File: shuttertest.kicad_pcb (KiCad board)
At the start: 2 copper layers, 52 x 101.3 mm, 74 parts, among them J1 Conn_01x20_Female, J2 Conn_01x06_Male, J3 Conn_01x06_Female, J4 Conn_01x06_Female, J5 Conn_01x06_Male, J6 Conn_01x06_Female, J7 Conn_01x06_Female, J8 AVR-ISP-6, SW1 SW_Push, U1 ATmega328PB-A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

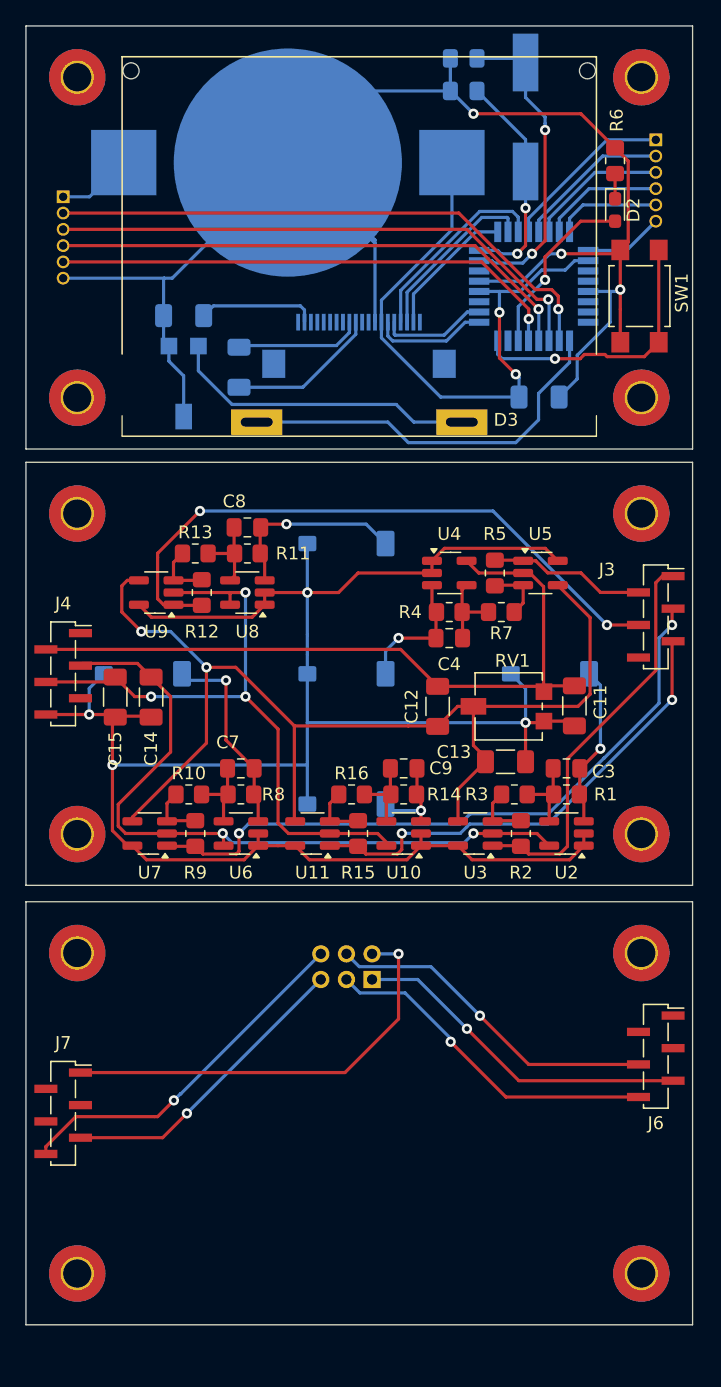
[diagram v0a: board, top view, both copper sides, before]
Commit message: Use through-hole connectors on bottom board
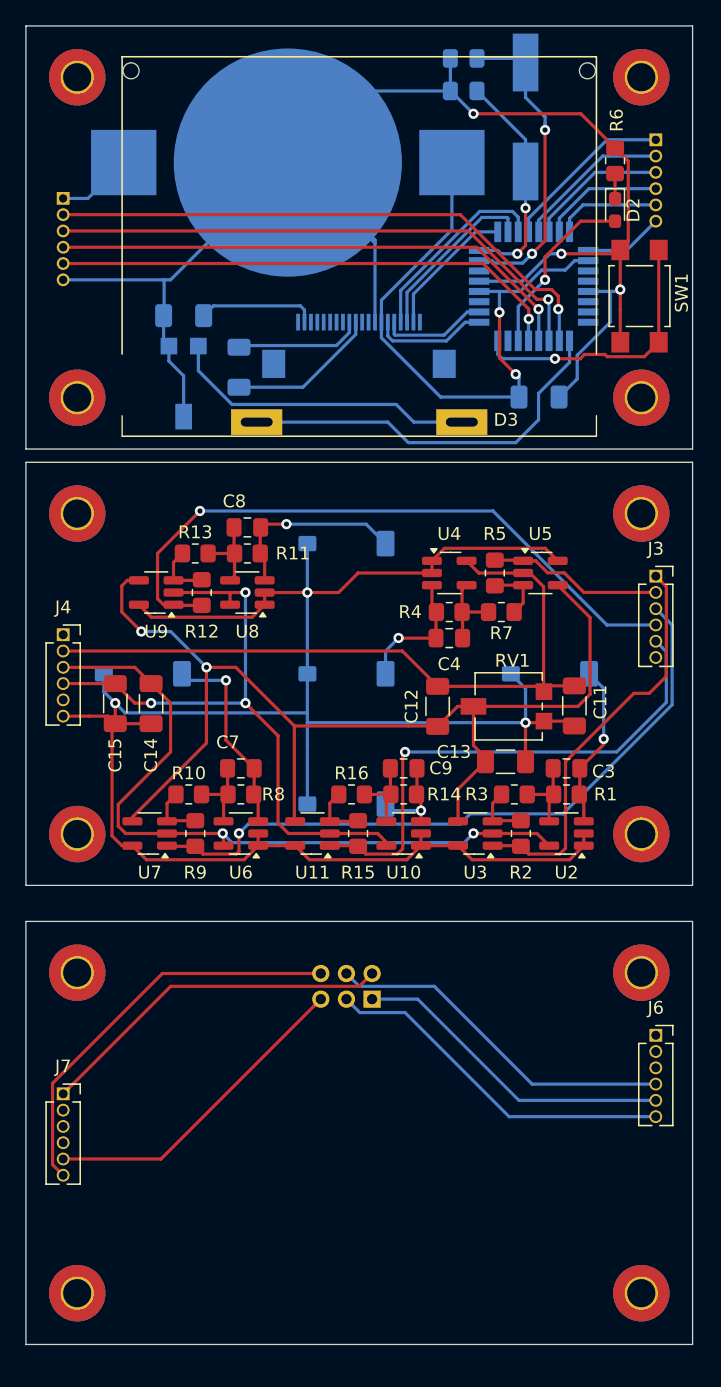
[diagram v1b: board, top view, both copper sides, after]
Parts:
- J3, J4, J6, J7: footprint Connector_PinSocket_1.27mm:PinSocket_1x06_P1.27mm_Vertical_SMD_Pin1Right -> Connector_PinSocket_1.27mm:PinSocket_1x06_P1.27mm_Vertical
- moved J3 3.18 mm to (124.0, 78.7)
- moved J4 3.05 mm to (77.7, 83.3)
- moved J6 1.64 mm to (124.0, 114.6)
- moved REF** 1.53 mm to (78.8, 134.7)
- moved REF** 1.53 mm to (122.8, 134.7)
- moved J8 1.53 mm to (101.8, 111.7)
- moved REF** 1.53 mm to (78.8, 109.7)
- moved REF** 1.53 mm to (122.8, 109.7)
- moved J7 1.51 mm to (77.7, 119.1)
- moved C14 0.51 mm to (84.6, 88.7)
- moved C15 0.51 mm to (81.8, 88.7)
- moved J5 0.13 mm to (77.7, 49.3)
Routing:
- net VDD: track 33.7 -> 28.0 mm, vias 1 -> 0
- net GND2: track 28.3 -> 32.0 mm, vias 1 -> 0
- net Net-(J3-Pin_5): track 37.2 -> 40.8 mm, vias 2 -> 1
- net unconnected-(C15-Pad1): track 51.4 -> 49.9 mm
- net VCC: track 57.9 -> 56.5 mm
- net unconnected-(J7-Pin_5-Pad5): track 23.9 -> 25.3 mm, vias 1 -> 0
- net Net-(J6-Pin_5): track 26.8 -> 25.4 mm, vias 1 -> 0
- net Net-(J6-Pin_4): track 26.4 -> 27.7 mm, vias 1 -> 0
- net Net-(J3-Pin_2): track 12.2 -> 13.6 mm
- net GND1: track 166.0 -> 164.8 mm, vias 4 -> 3
- net unconnected-(J6-Pin_6-Pad6): track 26.7 -> 27.9 mm, vias 1 -> 0
- net Net-(J3-Pin_3): track 52.2 -> 53.3 mm, vias 2 -> 1
- net unconnected-(C14-Pad1): track 56.4 -> 57.3 mm
- net Net-(J3-Pin_4): track 50.5 -> 51.1 mm, vias 2 -> 1
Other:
- board size 52 x 101.3 mm -> 52 x 102.9 mm

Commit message: Unify panel gap
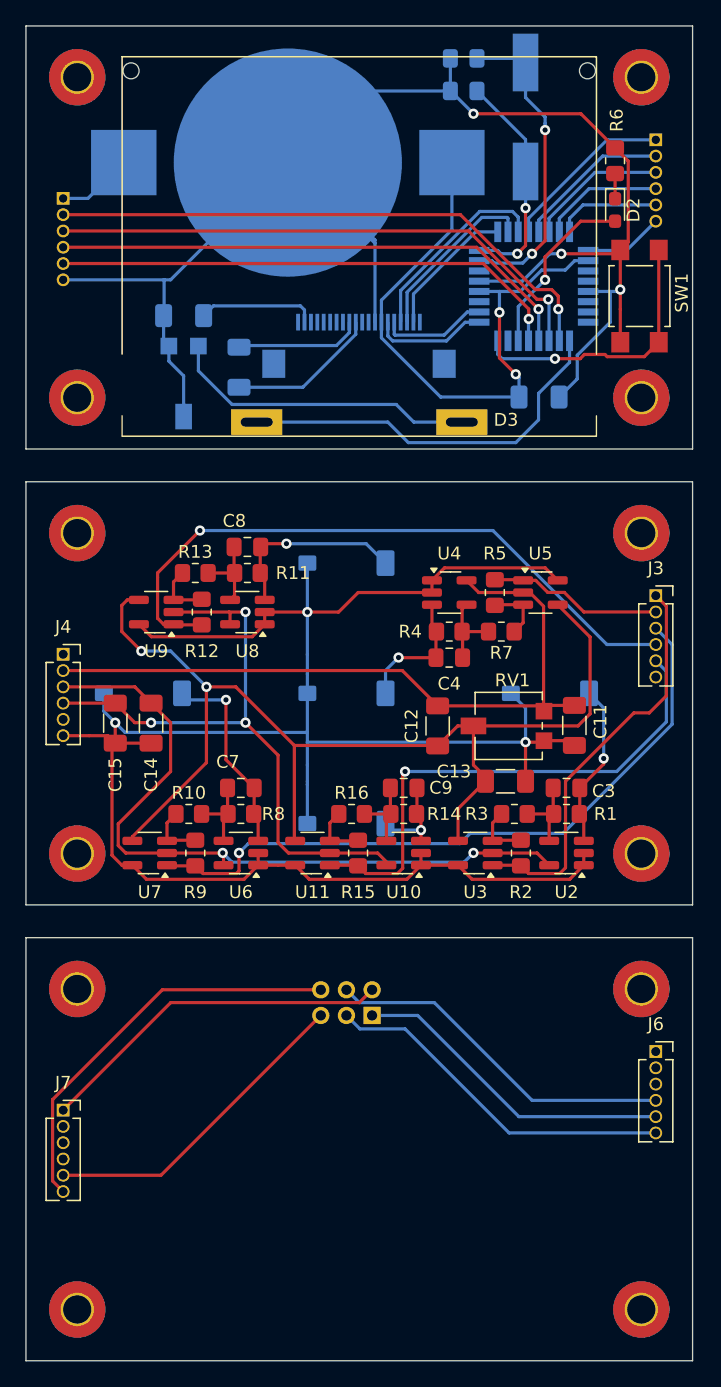
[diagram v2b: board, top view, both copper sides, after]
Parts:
- moved C12 1.52 mm to (106.9, 90.4)
- moved C13 1.52 mm to (112.2, 94.7)
- moved C14 1.52 mm to (84.6, 90.2)
- moved C15 1.52 mm to (81.8, 90.2)
- moved C3 1.52 mm to (117.0, 95.3)
- moved C4 1.52 mm to (107.8, 85.1)
- moved C7 1.52 mm to (91.6, 95.3)
- moved C8 1.52 mm to (92.1, 76.5)
- moved C9 1.52 mm to (104.3, 95.3)
- moved D1 1.52 mm to (115.7, 87.9)
- moved D4 1.52 mm to (99.8, 87.9)
- moved D5 1.52 mm to (83.9, 87.9)
- moved D6 1.52 mm to (99.8, 77.7)
- moved D7 1.52 mm to (99.8, 98.0)
- moved J3 1.52 mm to (124.0, 80.3)
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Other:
- board size 52 x 102.9 mm -> 52 x 104.1 mm

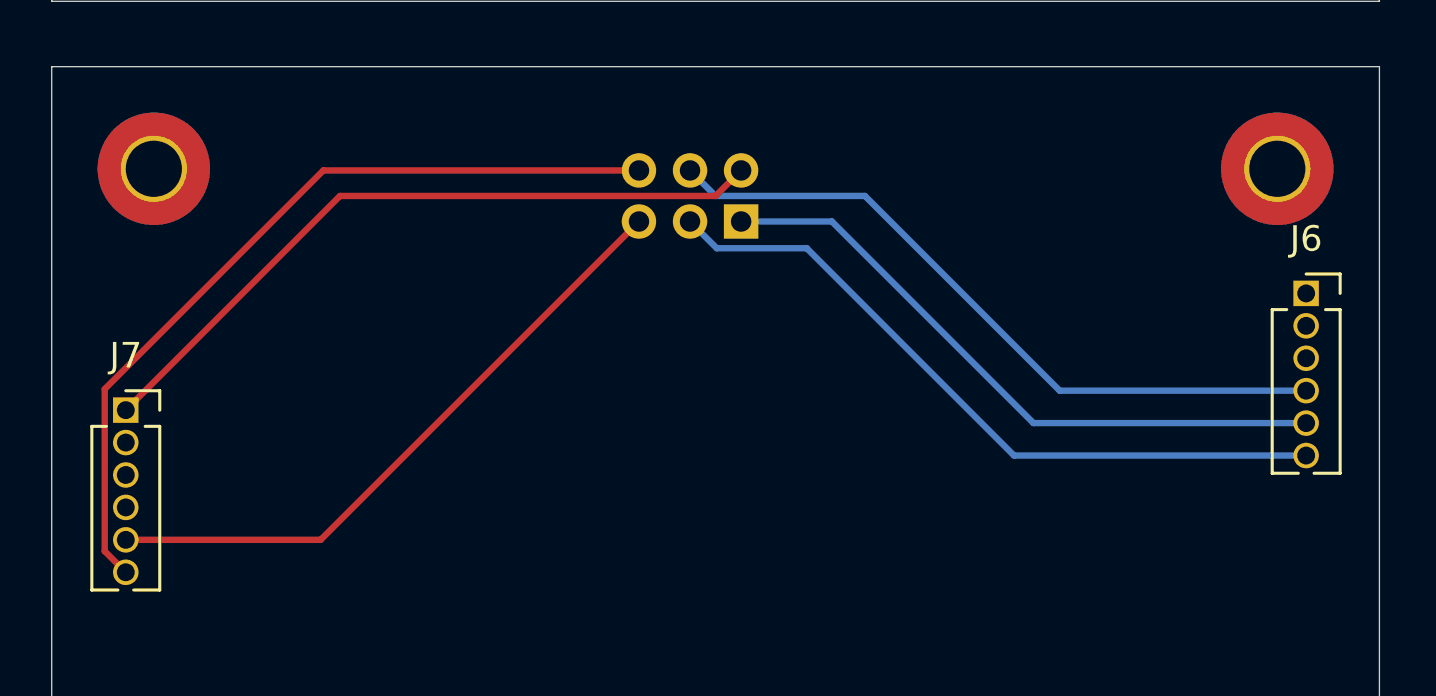
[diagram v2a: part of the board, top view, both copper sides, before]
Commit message: 2.54mm pitch AVR ISP header
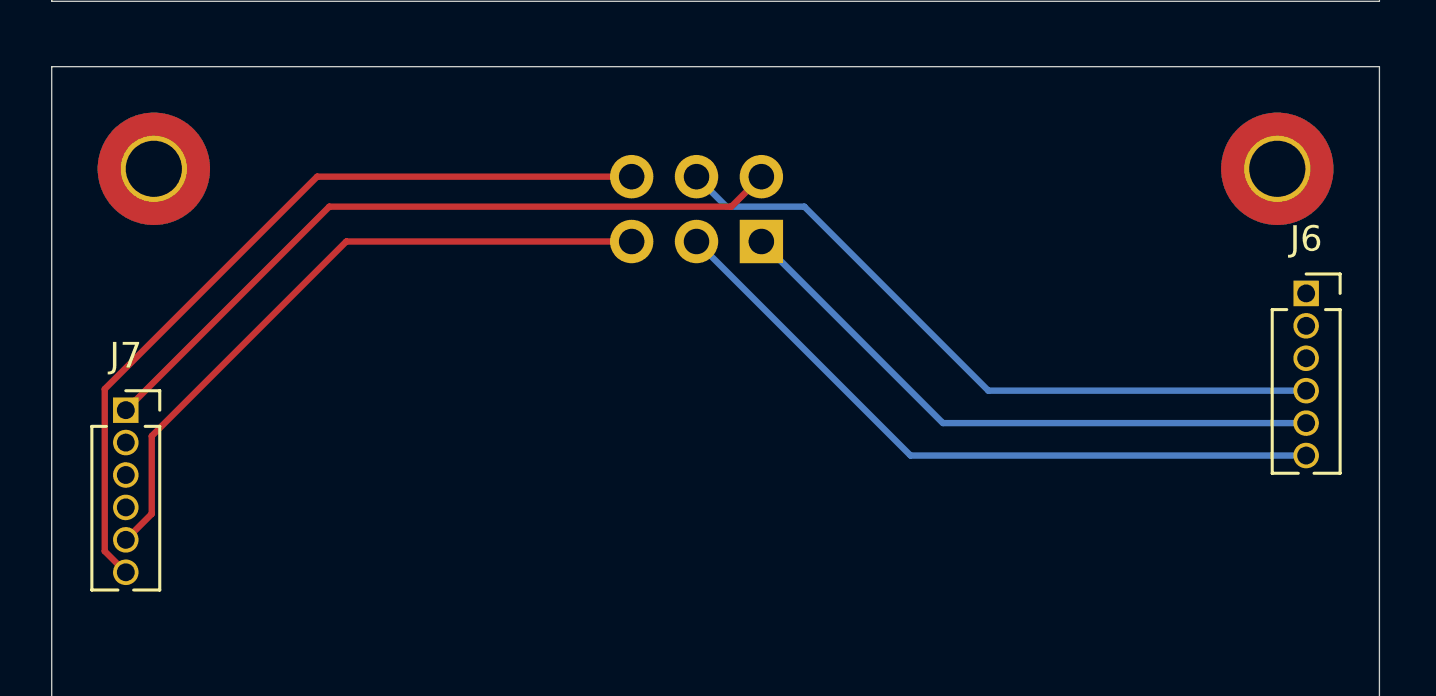
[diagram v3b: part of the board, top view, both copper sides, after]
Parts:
- J8: footprint Connector_PinHeader_2.00mm:PinHeader_2x03_P2.00mm_Vertical -> Connector_PinHeader_2.54mm:PinHeader_2x03_P2.54mm_Vertical
- moved J8 1.12 mm to (102.6, 113.8)
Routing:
- net unconnected-(J7-Pin_5-Pad5): track 25.3 -> 26.4 mm
- net Net-(J6-Pin_5): track 25.4 -> 24.3 mm
- net VDD: track 28.0 -> 28.7 mm
- net unconnected-(J6-Pin_6-Pad6): track 27.9 -> 27.3 mm
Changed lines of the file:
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@@
 		)
 	)
-	(footprint "Connector_PinHeader_2.00mm:PinHeader_2x03_P2.00mm_Vertical"
+	(footprint "Connector_PinHeader_2.54mm:PinHeader_2x03_P2.54mm_Vertical"
 		(layer "B.Cu")
-		(at 101.822 113.008 90)
-		(descr "Through hole straight pin header, 2x03, 2.00mm pitch, double rows")
-		(tags "Through hole pin header THT 2x03 2.00mm double row")
+		(at 102.616 113.792 90)
+		(descr "Through hole straight pin header, 2x03, 2.54mm pitch, double rows")
+		(tags "Through hole pin header THT 2x03 2.54mm double row")
 		(property "Reference" "J8"
-			(at 4.286 -1.746 0)
+			(at 1.27 2.33 -90)
 			(layer "B.SilkS")
 			(effects
@@
 		)
 		(property "Value" "AVR-ISP-6"
-			(at 1 -6.06 90)
+			(at 1.27 -7.41 -90)
 			(layer "B.Fab")
 			(effects
@@
 			)
 		)
-		(property "Footprint" "Connector_PinHeader_2.00mm:PinHeader_2x03_P2.00mm_Vertical"
+		(property "Footprint" "Connector_PinHeader_2.54mm:PinHeader_2x03_P2.54mm_Vertical"
 			(at 0 0 -90)
 			(unlocked yes)
@@
 		(attr through_hole)
 		(fp_line
-			(start 3.06 -5.06)
-			(end -1.06 -5.06)
+			(start 3.87 -6.41)
+			(end -1.33 -6.41)
 			(stroke
 				(width 0.12)
@@
 		)
 		(fp_line
-			(start 3.06 -5.06)
-			(end 3.06 1.06)
+			(start 3.87 -6.41)
+			(end 3.87 1.33)
 			(stroke
 				(width 0.12)
@@
 		)
 		(fp_line
-			(start -1.06 -5.06)
-			(end -1.06 -1)
+			(start -1.33 -6.41)
+			(end -1.33 -1.27)
 			(stroke
 				(width 0.12)
@@
 		)
 		(fp_line
-			(start 1 -1)
-			(end -1.06 -1)
+			(start 1.27 -1.27)
+			(end -1.33 -1.27)
 			(stroke
 				(width 0.12)
@@
 		)
 		(fp_line
-			(start 3.06 1.06)
-			(end 1 1.06)
+			(start 3.87 1.33)
+			(end 1.27 1.33)
 			(stroke
 				(width 0.12)
@@
 		)
 		(fp_line
-			(start 1 1.06)
-			(end 1 -1)
+			(start 1.27 1.33)
+			(end 1.27 -1.27)
 			(stroke
 				(width 0.12)
@@
 		)
 		(fp_line
-			(start 0 1.06)
-			(end -1.06 1.06)
+			(start 0 1.33)
+			(end -1.33 1.33)
 			(stroke
 				(width 0.12)
@@
 		)
 		(fp_line
-			(start -1.06 1.06)
-			(end -1.06 0)
+			(start -1.33 1.33)
+			(end -1.33 0)
 			(stroke
 				(width 0.12)
@@
 		)
 		(fp_line
-			(start 3.5 -5.5)
-			(end -1.5 -5.5)
+			(start 4.35 -6.85)
+			(end -1.8 -6.85)
 			(stroke
 				(width 0.05)
@@
 		)
 		(fp_line
-			(start -1.5 -5.5)
-			(end -1.5 1.5)
+			(start -1.8 -6.85)
+			(end -1.8 1.8)
 			(stroke
 				(width 0.05)
@@
 		)
 		(fp_line
-			(start 3.5 1.5)
-			(end 3.5 -5.5)
+			(start 4.35 1.8)
+			(end 4.35 -6.85)
 			(stroke
 				(width 0.05)
@@
 		)
 		(fp_line
-			(start -1.5 1.5)
-			(end 3.5 1.5)
+			(start -1.8 1.8)
+			(end 4.35 1.8)
 			(stroke
 				(width 0.05)
@@
 		)
 		(fp_line
-			(start 3 -5)
-			(end 3 1)
+			(start 3.81 -6.35)
+			(end 3.81 1.27)
 			(stroke
 				(width 0.1)
@@
 		)
 		(fp_line
-			(start -1 -5)
-			(end 3 -5)
+			(start -1.27 -6.35)
+			(end 3.81 -6.35)
 			(stroke
 				(width 0.1)
@@
 		)
 		(fp_line
-			(start -1 0)
-			(end -1 -5)
+			(start -1.27 0)
+			(end -1.27 -6.35)
 			(stroke
 				(width 0.1)
@@
 		)
 		(fp_line
-			(start 3 1)
-			(end 0 1)
+			(start 3.81 1.27)
+			(end 0 1.27)
 			(stroke
 				(width 0.1)
@@
 		)
 		(fp_line
-			(start 0 1)
-			(end -1 0)
+			(start 0 1.27)
+			(end -1.27 0)
 			(stroke
 				(width 0.1)
@@
 		)
 		(fp_text user "${REFERENCE}"
-			(at 1 -2 0)
+			(at 1.27 -2.54 0)
 			(layer "B.Fab")
 			(effects
@@
 		(pad "1" thru_hole rect
 			(at 0 0 90)
-			(size 1.35 1.35)
-			(drill 0.8)
+			(size 1.7 1.7)
+			(drill 1)
 			(layers "*.Cu" "*.Mask")
 			(remove_unused_layers no)
@@
 		)
 		(pad "2" thru_hole oval
-			(at 2 0 90)
-			(size 1.35 1.35)
-			(drill 0.8)
+			(at 2.54 0 90)
+			(size 1.7 1.7)
+			(drill 1)
 			(layers "*.Cu" "*.Mask")
 			(remove_unused_layers no)
@@
 		)
 		(pad "3" thru_hole oval
-			(at 0 -2 90)
-			(size 1.35 1.35)
-			(drill 0.8)
+			(at 0 -2.54 90)
+			(size 1.7 1.7)
+			(drill 1)
 			(layers "*.Cu" "*.Mask")
 			(remove_unused_layers no)
@@
 		)
 		(pad "4" thru_hole oval
-			(at 2 -2 90)
-			(size 1.35 1.35)
-			(drill 0.8)
+			(at 2.54 -2.54 90)
+			(size 1.7 1.7)
+			(drill 1)
 			(layers "*.Cu" "*.Mask")
 			(remove_unused_layers no)
@@
 		)
 		(pad "5" thru_hole oval
-			(at 0 -4 90)
-			(size 1.35 1.35)
-			(drill 0.8)
+			(at 0 -5.08 90)
+			(size 1.7 1.7)
+			(drill 1)
 			(layers "*.Cu" "*.Mask")
 			(remove_unused_layers no)
@@
 		)
 		(pad "6" thru_hole oval
-			(at 2 -4 90)
-			(size 1.35 1.35)
-			(drill 0.8)
+			(at 2.54 -5.08 90)
+			(size 1.7 1.7)
+			(drill 1)
 			(layers "*.Cu" "*.Mask")
 			(remove_unused_layers no)
@@
 			(pintype "passive")
 		)
-		(model "${KICAD8_3DMODEL_DIR}/Connector_PinHeader_2.00mm.3dshapes/PinHeader_2x03_P2.00mm_Vertical.wrl"
+		(model "${KICAD8_3DMODEL_DIR}/Connector_PinHeader_2.54mm.3dshapes/PinHeader_2x03_P2.54mm_Vertical.wrl"
 			(offset
 				(xyz 0 0 0)
@@
 	)
 	(segment
-		(start 105.378 113.008)
-		(end 113.274 120.904)
+		(start 123.952 120.904)
+		(end 109.728 120.904)
 		(width 0.25)
 		(layer "B.Cu")
@@
 	)
 	(segment
-		(start 101.822 113.008)
-		(end 105.378 113.008)
+		(start 109.728 120.904)
+		(end 102.616 113.792)
 		(width 0.25)
 		(layer "B.Cu")
@@
 	)
 	(segment
-		(start 113.274 120.904)
-		(end 123.952 120.904)
-		(width 0.25)
-		(layer "B.Cu")
-		(net 75)
-	)
-	(segment
-		(start 100.87 114.056)
-		(end 104.394 114.056)
+		(start 108.458 122.174)
+		(end 100.076 113.792)
 		(width 0.25)
 		(layer "B.Cu")
@@
 	)
 	(segment
-		(start 99.822 113.008)
-		(end 100.87 114.056)
+		(start 123.952 122.174)
+		(end 108.458 122.174)
 		(width 0.25)
 		(layer "B.Cu")
@@
 	)
 	(segment
-		(start 112.512 122.174)
-		(end 123.952 122.174)
+		(start 111.506 119.634)
+		(end 123.952 119.634)
 		(width 0.25)
 		(layer "B.Cu")
-		(net 76)
-	)
-	(segment
-		(start 104.394 114.056)
-		(end 112.512 122.174)
-		(width 0.25)
-		(layer "B.Cu")
-		(net 76)
+		(net 78)
 	)
 	(segment
-		(start 123.952 119.634)
-		(end 114.3 119.634)
+		(start 104.299 112.427)
+		(end 111.506 119.634)
 		(width 0.25)
 		(layer "B.Cu")
@@
 	)
 	(segment
-		(start 100.822 112.008)
-		(end 99.822 111.008)
+		(start 101.251 112.427)
+		(end 104.299 112.427)
 		(width 0.25)
 		(layer "B.Cu")
@@
 	)
 	(segment
-		(start 114.3 119.634)
-		(end 106.674 112.008)
+		(start 100.076 111.252)
+		(end 101.251 112.427)
 		(width 0.25)
 		(layer "B.Cu")
@@
 	)
 	(segment
-		(start 106.674 112.008)
-		(end 100.822 112.008)
+		(start 86.36 113.792)
+		(end 78.74 121.412)
 		(width 0.25)
-		(layer "B.Cu")
-		(net 78)
+		(layer "F.Cu")
+		(net 80)
 	)
 	(segment
-		(start 77.724 125.476)
-		(end 85.354 125.476)
+		(start 78.74 121.412)
+		(end 78.74 124.46)
 		(width 0.25)
 		(layer "F.Cu")
@@
 	)
 	(segment
-		(start 85.354 125.476)
-		(end 97.822 113.008)
+		(start 97.536 113.792)
+		(end 86.36 113.792)
 		(width 0.25)
 		(layer "F.Cu")
@@
 	)
 	(segment
-		(start 85.462 111.008)
-		(end 97.822 111.008)
+		(start 78.74 124.46)
+		(end 77.724 125.476)
 		(width 0.25)
 		(layer "F.Cu")
-		(net 83)
+		(net 80)
 	)
 	(segment
 		(start 76.899 119.571)
-		(end 85.462 111.008)
+		(end 85.218 111.252)
 		(width 0.25)
 		(layer "F.Cu")
@@
 	)
 	(segment
-		(start 86.112 112.008)
-		(end 100.822 112.008)
+		(start 85.218 111.252)
+		(end 97.536 111.252)
 		(width 0.25)
 		(layer "F.Cu")
-		(net 84)
+		(net 83)
 	)
 	(segment
 		(start 77.724 120.396)
-		(end 86.112 112.008)
+		(end 85.693 112.427)
+		(width 0.25)
+		(layer "F.Cu")
+		(net 84)
+	)
+	(segment
+		(start 85.693 112.427)
+		(end 101.441 112.427)
 		(width 0.25)
 		(layer "F.Cu")
@@
 	)
 	(segment
-		(start 100.822 112.008)
-		(end 101.822 111.008)
+		(start 101.441 112.427)
+		(end 102.616 111.252)
 		(width 0.25)
 		(layer "F.Cu")
